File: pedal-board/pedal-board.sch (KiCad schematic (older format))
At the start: 55 parts, among them J1 AudioJack0, J10 CH7, J11 CH7, J2 AudioJack1, J3 AudioJack2, J4 AudioJack3, J5 Qwiic, J6 CH7, J7 CH7, J8 CH7, J9 CH7, U1 ADS7830

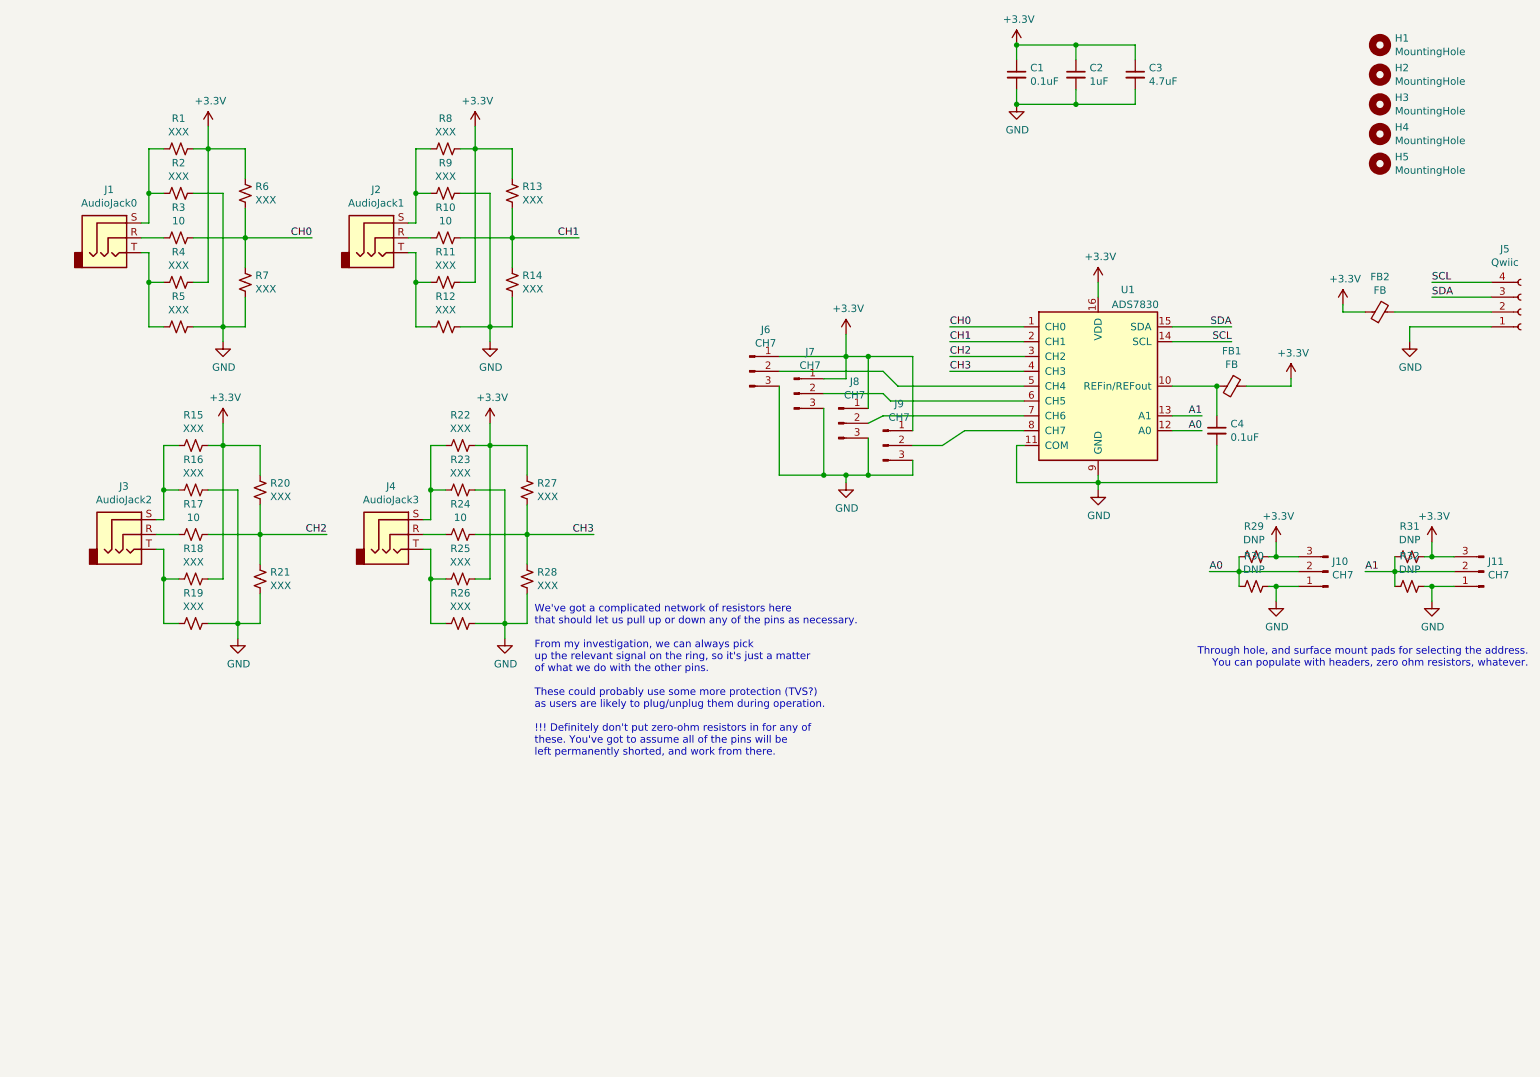
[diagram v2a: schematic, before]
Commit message: Second Qwiic header, semi-split analog power rail, silkscreen tweaks.
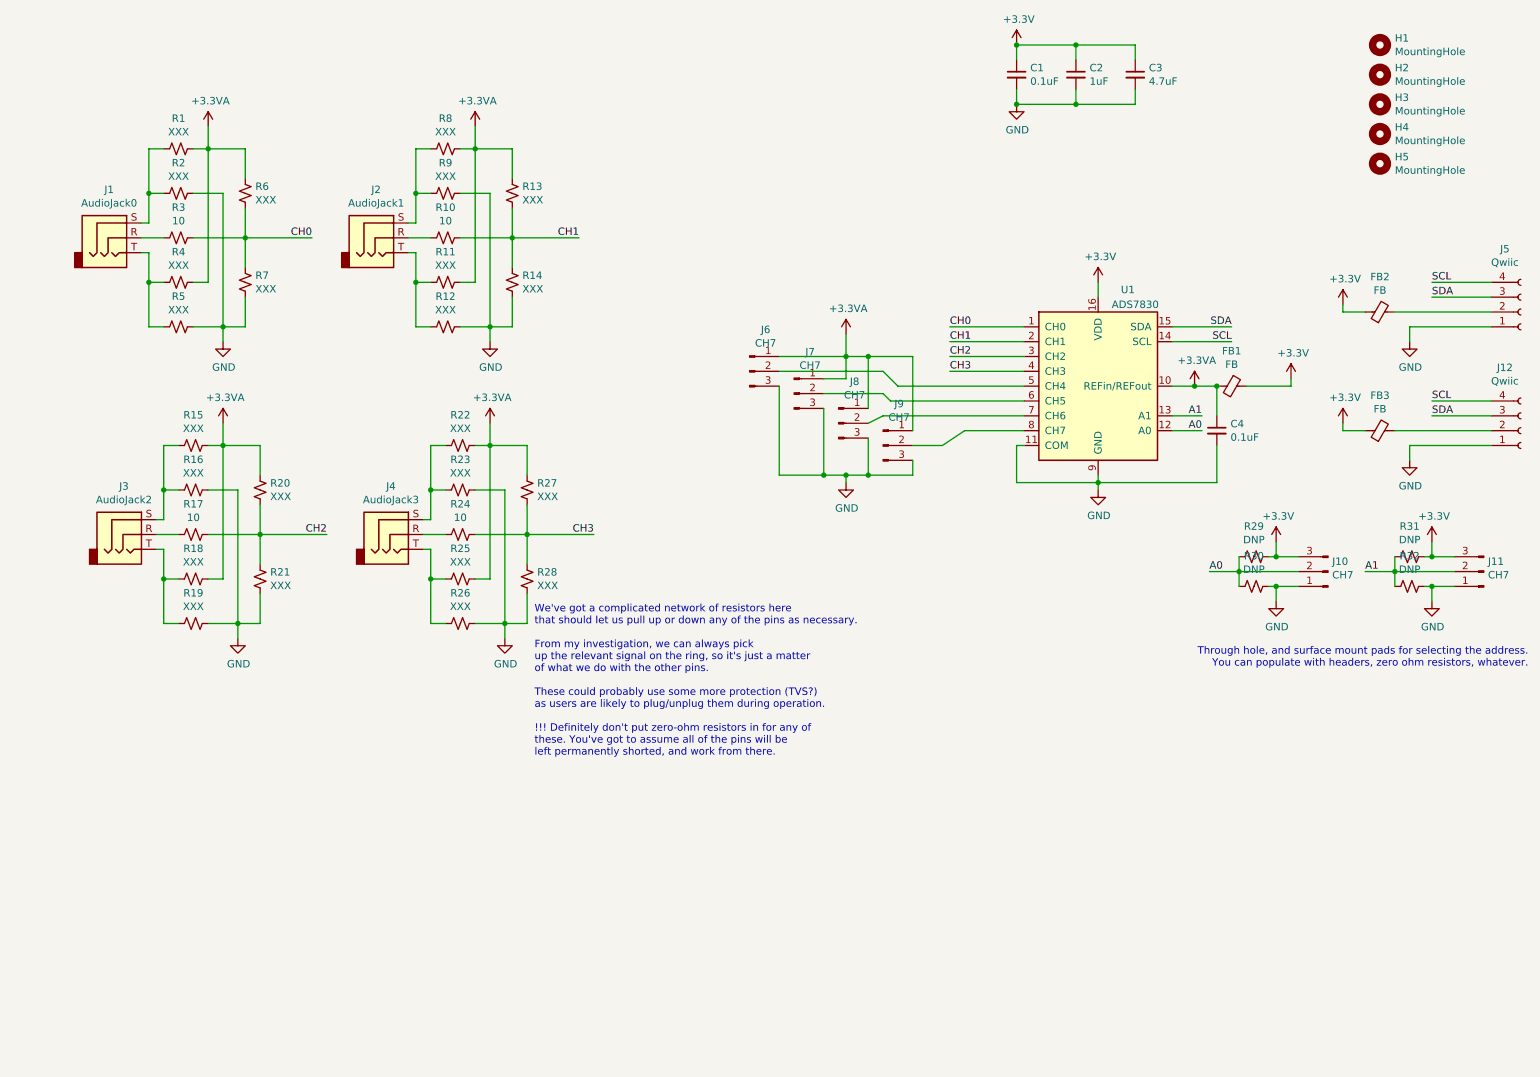
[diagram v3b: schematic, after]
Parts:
- added FB3: FB, Inductors_SMD:L_0805_HandSoldering, symbol Device:Ferrite_Bead_Small
- added J12: Qwiic, Connectors_JST:JST_SH_SM04B-SRSS-TB_04x1.00mm_Angled, symbol Connector:Conn_01x04_Female
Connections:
- net +3V3: now also FB3.1; no longer J6.1 (Pin_1), J7.1 (Pin_1), J8.1 (Pin_1), J9.1 (Pin_1), R1.2, R11.2, R13.1, R15.2, R18.2, R20.1, R22.2, R25.2, R27.1, R4.2, R6.1, R8.2
- net GND: now also J12.1 (Pin_1)
- net SCL: now also J12.4 (Pin_4)
- net SDA: now also J12.3 (Pin_3)
- net +3.3VA: now reaches C4.1, FB1.2, U1.10 (REFin/REFout)
- net +3.3VA: now also J6.1 (Pin_1), J7.1 (Pin_1), J8.1 (Pin_1), J9.1 (Pin_1), R1.2, R11.2, R13.1, R15.2, R18.2, R20.1, R22.2, R25.2, R27.1, R4.2, R6.1, R8.2
- new net: FB3.2, J12.2 (Pin_2)
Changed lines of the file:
@@
 	2100 2350 2100 1450
 Connection ~ 2100 1450
-$Comp
-L power:+3.3V #PWR01
-U 1 1 5FD723D3
-P 2100 1300
-F 0 "#PWR01" H 2100 1150 50  0001 C CNN
-F 1 "+3.3V" H 2115 1473 50  0000 C CNN
-F 2 "" H 2100 1300 50  0001 C CNN
-F 3 "" H 2100 1300 50  0001 C CNN
-	1    2100 1300
-	1    0    0    -1
-$EndComp
 Wire Wire Line
 	7600 2650 7100 2650
@@
 Connection ~ 3900 1450
 $Comp
-L power:+3.3V #PWR0102
-U 1 1 5FDA75CC
-P 3900 1300
-F 0 "#PWR0102" H 3900 1150 50  0001 C CNN
-F 1 "+3.3V" H 3915 1473 50  0000 C CNN
-F 2 "" H 3900 1300 50  0001 C CNN
-F 3 "" H 3900 1300 50  0001 C CNN
-	1    3900 1300
-	1    0    0    -1
-$EndComp
-$Comp
 L Device:R_Small_US R13
 U 1 1 5FDA75D2
@@
 Connection ~ 2200 3450
 $Comp
-L power:+3.3V #PWR0104
-U 1 1 5FDAFA8A
-P 2200 3300
-F 0 "#PWR0104" H 2200 3150 50  0001 C CNN
-F 1 "+3.3V" H 2215 3473 50  0000 C CNN
-F 2 "" H 2200 3300 50  0001 C CNN
-F 3 "" H 2200 3300 50  0001 C CNN
-	1    2200 3300
-	1    0    0    -1
-$EndComp
-$Comp
 L Device:R_Small_US R20
 U 1 1 5FDAFA90
@@
 Connection ~ 4000 3450
 $Comp
-L power:+3.3V #PWR0106
-U 1 1 5FDB7BAA
-P 4000 3300
-F 0 "#PWR0106" H 4000 3150 50  0001 C CNN
-F 1 "+3.3V" H 4015 3473 50  0000 C CNN
-F 2 "" H 4000 3300 50  0001 C CNN
-F 3 "" H 4000 3300 50  0001 C CNN
-	1    4000 3300
-	1    0    0    -1
-$EndComp
-$Comp
 L Device:R_Small_US R27
 U 1 1 5FDB7BB0
@@
 $EndComp
 Wire Wire Line
-	8600 3050 8900 3050
+	8600 3050 8750 3050
 Wire Wire Line
 	8900 3050 8900 3250
@@
 Wire Wire Line
 	6750 3050 7600 3050
-$Comp
-L power:+3.3V #PWR0112
-U 1 1 5FDC259C
-P 6400 2700
-F 0 "#PWR0112" H 6400 2550 50  0001 C CNN
-F 1 "+3.3V" H 6415 2873 50  0000 C CNN
-F 2 "" H 6400 2700 50  0001 C CNN
-F 3 "" H 6400 2700 50  0001 C CNN
-	1    6400 2700
-	1    0    0    -1
-$EndComp
 Wire Wire Line
 	5950 2850 6400 2850
@@
 Text Notes 11000 4950 2    50   ~ 0
 Through hole, and surface mount pads for selecting the address.\nYou can populate with headers, zero ohm resistors, whatever.
+$Comp
+L power:+3.3VA #PWR0112
+U 1 1 5FDCC422
+P 8750 3050
+F 0 "#PWR0112" H 8750 2900 50  0001 C CNN
+F 1 "+3.3VA" H 8765 3223 50  0000 C CNN
+F 2 "" H 8750 3050 50  0001 C CNN
+F 3 "" H 8750 3050 50  0001 C CNN
+	1    8750 3050
+	1    0    0    -1
+$EndComp
+Connection ~ 8750 3050
+Wire Wire Line
+	8750 3050 8900 3050
+$Comp
+L power:+3.3VA #PWR0118
+U 1 1 5FDCD03F
+P 6400 2700
+F 0 "#PWR0118" H 6400 2550 50  0001 C CNN
+F 1 "+3.3VA" H 6415 2873 50  0000 C CNN
+F 2 "" H 6400 2700 50  0001 C CNN
+F 3 "" H 6400 2700 50  0001 C CNN
+	1    6400 2700
+	1    0    0    -1
+$EndComp
+$Comp
+L power:+3.3VA #PWR0102
+U 1 1 5FDCDDF7
+P 4000 3300
+F 0 "#PWR0102" H 4000 3150 50  0001 C CNN
+F 1 "+3.3VA" H 4015 3473 50  0000 C CNN
+F 2 "" H 4000 3300 50  0001 C CNN
+F 3 "" H 4000 3300 50  0001 C CNN
+	1    4000 3300
+	1    0    0    -1
+$EndComp
+$Comp
+L power:+3.3VA #PWR0104
+U 1 1 5FDCE658
+P 2200 3300
+F 0 "#PWR0104" H 2200 3150 50  0001 C CNN
+F 1 "+3.3VA" H 2215 3473 50  0000 C CNN
+F 2 "" H 2200 3300 50  0001 C CNN
+F 3 "" H 2200 3300 50  0001 C CNN
+	1    2200 3300
+	1    0    0    -1
+$EndComp
+$Comp
+L power:+3.3VA #PWR0106
+U 1 1 5FDCED98
+P 2100 1300
+F 0 "#PWR0106" H 2100 1150 50  0001 C CNN
+F 1 "+3.3VA" H 2115 1473 50  0000 C CNN
+F 2 "" H 2100 1300 50  0001 C CNN
+F 3 "" H 2100 1300 50  0001 C CNN
+	1    2100 1300
+	1    0    0    -1
+$EndComp
+$Comp
+L power:+3.3VA #PWR0119
+U 1 1 5FDCF77F
+P 3900 1300
+F 0 "#PWR0119" H 3900 1150 50  0001 C CNN
+F 1 "+3.3VA" H 3915 1473 50  0000 C CNN
+F 2 "" H 3900 1300 50  0001 C CNN
+F 3 "" H 3900 1300 50  0001 C CNN
+	1    3900 1300
+	1    0    0    -1
+$EndComp
+$Comp
+L power:+3.3V #PWR0120
+U 1 1 5FDF7A0D
+P 9750 3300
+F 0 "#PWR0120" H 9750 3150 50  0001 C CNN
+F 1 "+3.3V" H 9765 3473 50  0000 C CNN
+F 2 "" H 9750 3300 50  0001 C CNN
+F 3 "" H 9750 3300 50  0001 C CNN
+	1    9750 3300
+	1    0    0    -1
+$EndComp
+$Comp
+L power:GND #PWR0121
+U 1 1 5FDF7A13
+P 10200 3550
+F 0 "#PWR0121" H 10200 3300 50  0001 C CNN
+F 1 "GND" H 10205 3377 50  0000 C CNN
+F 2 "" H 10200 3550 50  0001 C CNN
+F 3 "" H 10200 3550 50  0001 C CNN
+	1    10200 3550
+	1    0    0    -1
+$EndComp
+$Comp
+L Connector:Conn_01x04_Female J12
+U 1 1 5FDF7A19
+P 10950 3350
+F 0 "J12" H 10842 2925 50  0000 C CNN
+F 1 "Qwiic" H 10842 3016 50  0000 C CNN
+F 2 "Connectors_JST:JST_SH_SM04B-SRSS-TB_04x1.00mm_Angled" H 10950 3350 50  0001 C CNN
+F 3 "~" H 10950 3350 50  0001 C CNN
+	1    10950 3350
+	1    0    0    1
+$EndComp
+Wire Wire Line
+	9750 3300 9750 3350
+Wire Wire Line
+	9750 3350 9900 3350
+Wire Wire Line
+	10750 3450 10200 3450
+Wire Wire Line
+	10200 3450 10200 3550
+Wire Wire Line
+	10750 3250 10350 3250
+Wire Wire Line
+	10750 3150 10350 3150
+Text Label 10350 3150 0    50   ~ 0
+SCL
+Text Label 10350 3250 0    50   ~ 0
+SDA
+$Comp
+L Device:Ferrite_Bead_Small FB3
+U 1 1 5FDF7A27
+P 10000 3350
+F 0 "FB3" V 10237 3350 50  0000 C CNN
+F 1 "FB" V 10146 3350 50  0000 C CNN
+F 2 "Inductors_SMD:L_0805_HandSoldering" V 9930 3350 50  0001 C CNN
+F 3 "~" H 10000 3350 50  0001 C CNN
+	1    10000 3350
+	0    -1   -1   0
+$EndComp
+Wire Wire Line
+	10750 3350 10100 3350
 $EndSCHEMATC

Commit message: Rev 1 first batch of changes
- Made it narrower, but had to expand the space between mounting holes.
- Moved the jacks back 2.3mm.
- 10mm to board edge, 5mm clearance on the inside of the board, 7.5mm clearance on either side
- Fixed the outline to be silkscreen, not a hole in the mask
- Added I2C bus header
- Made nice little three pad footprints for spots where you need a pull up or a pull down.
- Drastically increased the space between the Qwiic headers
- On the pedal jacks, the signal is really on the Tip, not the ring where I had it. Not sure what I was thinking.
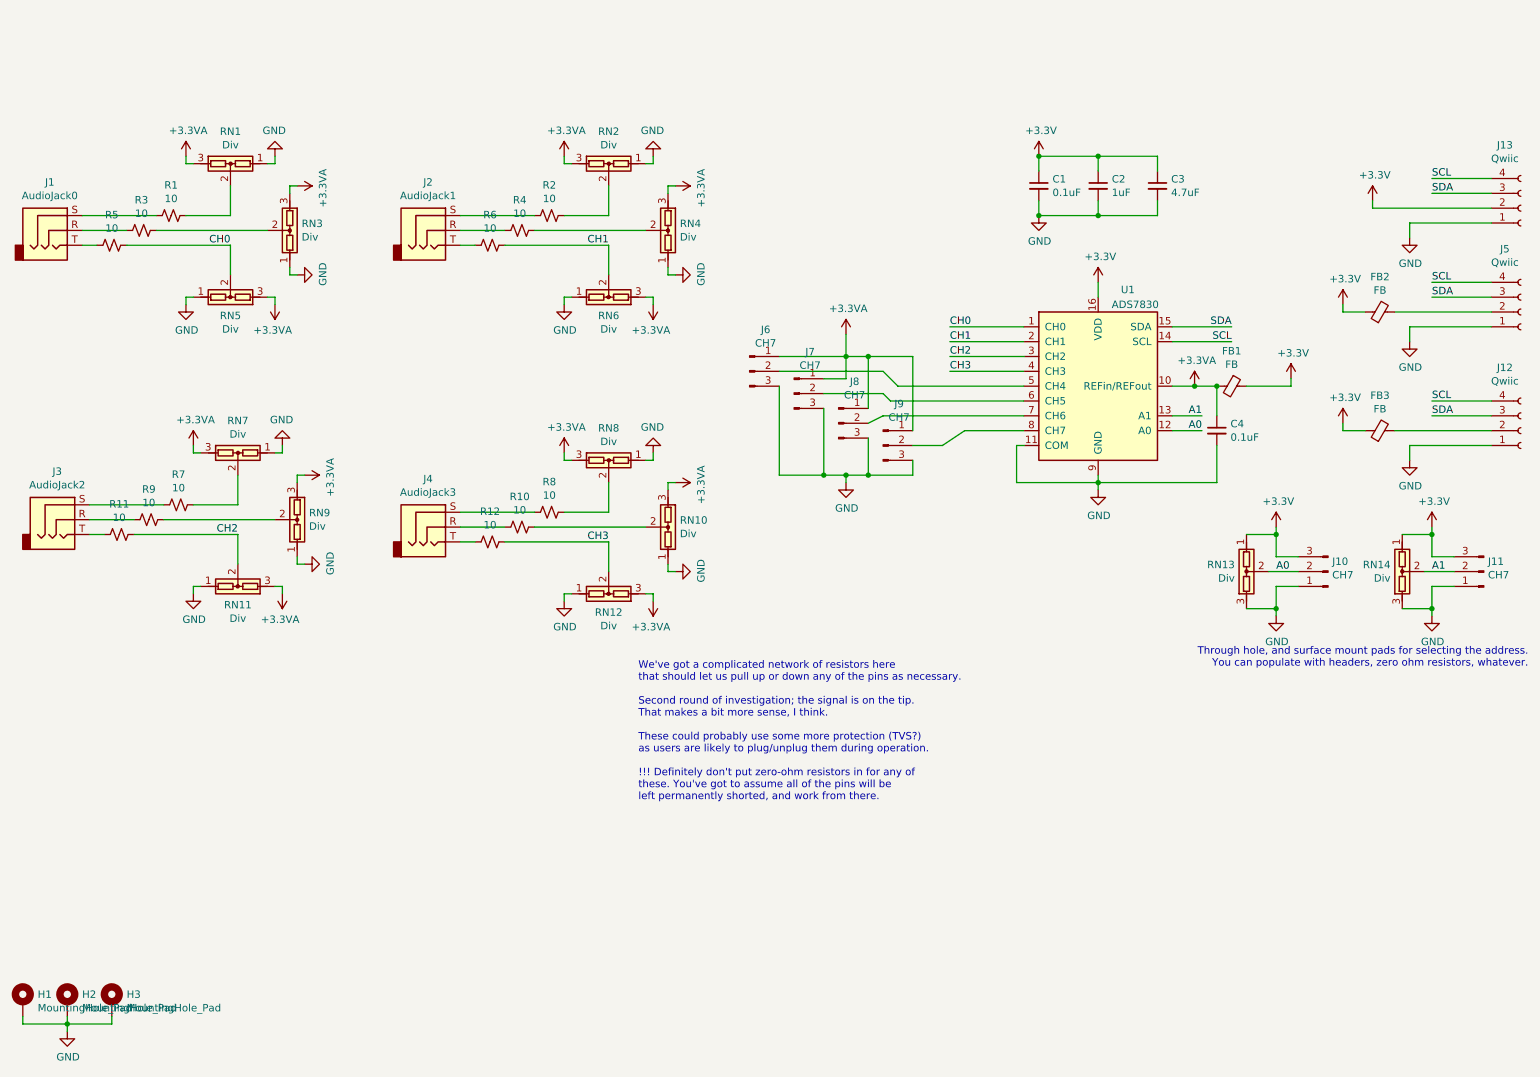
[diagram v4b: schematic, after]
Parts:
- removed H1, H2, H3, H4, H5: MountingHole, Mounting_Holes:MountingHole_3.2mm_M3, symbol Mechanical:MountingHole
- removed R13, R14, R15, R16, R18, R19, R20, R21, R22, R23, R25, R26, R27, R28: XXX, Resistors_SMD:R_0805_HandSoldering, symbol Device:R_Small_US
- removed R17, R24: 10, Resistors_SMD:R_0805_HandSoldering, symbol Device:R_Small_US
- removed R29, R30, R31, R32: DNP, Resistors_SMD:R_0805_HandSoldering, symbol Device:R_Small_US
- added H1, H2, H3: MountingHole_Pad, Mounting_Holes:MountingHole_3.2mm_M3_Pad_Via, symbol Mechanical:MountingHole_Pad
- added J13: Qwiic, Pin_Headers:Pin_Header_Straight_1x04_Pitch2.54mm, symbol Connector:Conn_01x04_Female
- added RN1, RN10, RN11, RN12, RN13, RN14, RN2, RN3, RN4, RN5, RN6, RN7, RN8, RN9: Div, footprints:R_0805_Divider, symbol Device:Voltage_Divider
- R1, R11, R12, R2, R4, R5, R6, R7, R8, R9: value XXX -> 10
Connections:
- net +3.3VA: now also RN1.3, RN10.3, RN11.3, RN12.3, RN2.3, RN3.3, RN4.3, RN5.3, RN6.3, RN7.3, RN8.3, RN9.3; no longer R1.2, R11.2, R4.2, R6.1, R8.2
- net +3V3: now also J13.2 (Pin_2), RN13.1, RN14.1
- net A0: now also RN13.2
- net A1: now also RN14.2
- net CH0: now also R5.1, RN5.2; no longer R3.1, R6.2, R7.1
- net CH1: now also R6.1, RN6.2; no longer R10.1
- net CH2: now also R11.1, RN11.2
- net CH3: now also R12.1, RN12.2
- net GND: now also H1.1, H2.1, H3.1, J13.1 (Pin_1), RN1.1, RN10.1, RN11.1, RN12.1, RN13.3, RN14.3, RN2.1, RN3.1, RN4.1, RN5.1, RN6.1, RN7.1, RN8.1, RN9.1; no longer R12.2, R2.2, R5.2, R7.2, R9.2
- net SCL: now also J13.4 (Pin_4)
- net SDA: now also J13.3 (Pin_3)
- net at J2.R: now also R4.2; no longer R10.2
- net at J3.R: now also R9.2
- net at J3.S: now also R7.2
- net at J3.T: now also R11.2
- net at J4.R: now also R10.2
- net at J4.S: now also R8.2
- net at J4.T: now also R12.2
- new net: J1.S, R1.2
- new net: J1.T, R5.2
- new net: J2.S, R2.2
- new net: J2.T, R6.2
- new net: R3.1, RN3.2
- new net: R1.1, RN1.2
- new net: R4.1, RN4.2
- new net: R2.1, RN2.2
- new net: R9.1, RN9.2
- new net: R7.1, RN7.2
- new net: R10.1, RN10.2
- new net: R8.1, RN8.2
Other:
- note added: "We've got a complicated network of resistors here\nthat should let us pull up or down any of the pins as necessary.\n\nSecond round of investigation; the signal is on the tip.\nThat makes a bit more sense, I think.\n\nThese could probably use some more protection (TVS?)\nas users are likely to plug/unplug them during operation.\n\n!!! Definitely don't put zero-ohm resistors in for any of\nthese. 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"
- note removed: "We've got a complicated network of resistors here\nthat should let us pull up or down any of the pins as necessary.\n\nFrom my investigation, we can always pick\nup the relevant signal on the ring, so it's just a matter\nof what we do with the other pins.\n\nThese could probably use some more protection (TVS?)\nas users are likely to plug/unplug them during operation.\n\n!!! Definitely don't put 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"
- moved on the sheet: C1, C2, C3, J1, J2, J3, J4
